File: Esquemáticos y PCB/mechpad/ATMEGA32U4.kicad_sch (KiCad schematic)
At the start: 22 parts

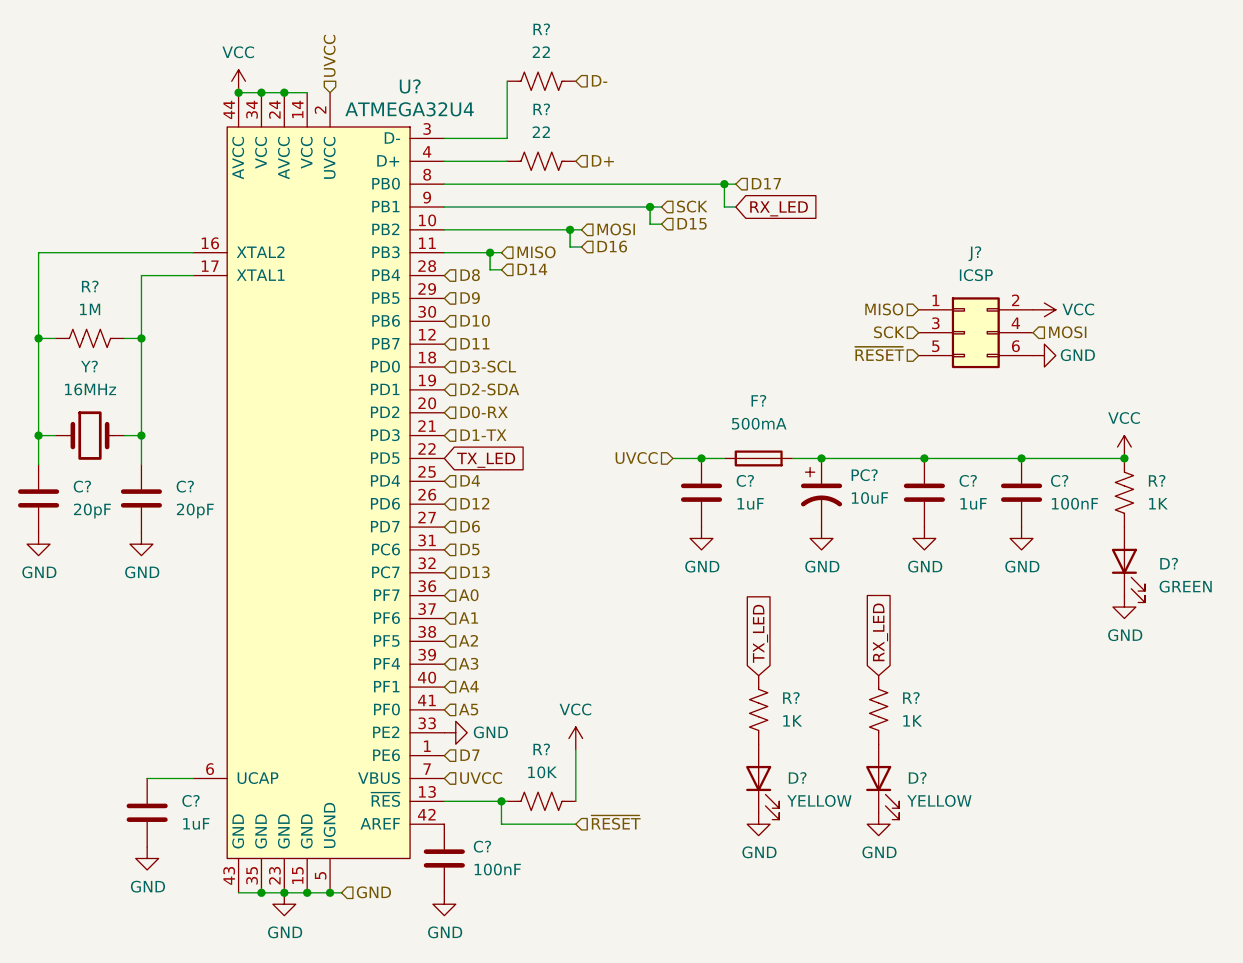
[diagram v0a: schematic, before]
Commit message: Updated schematic
Added connections between hierarchical sheets, more code testing
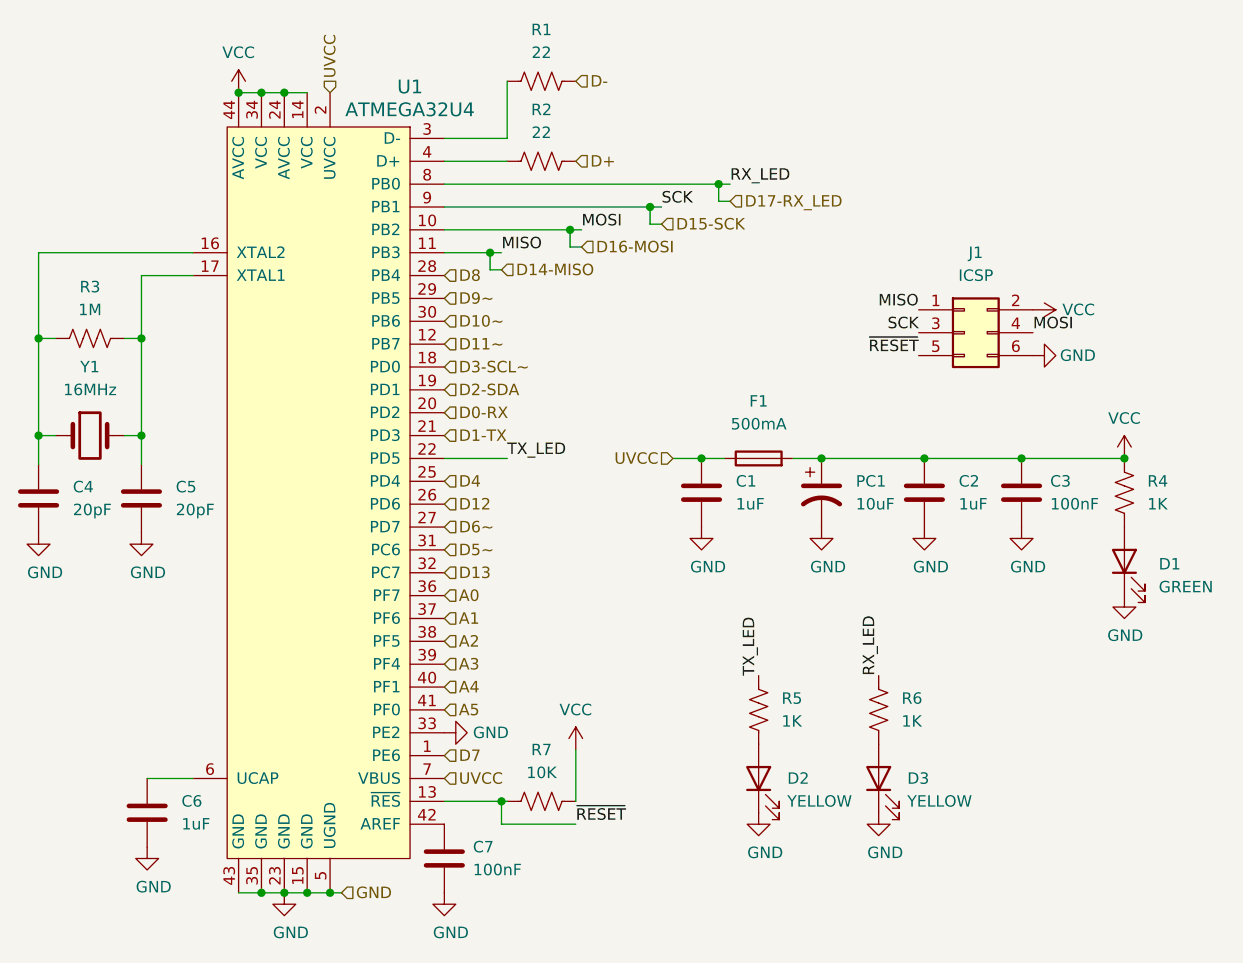
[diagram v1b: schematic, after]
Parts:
- gave numbers to parts that had none: 22
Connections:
- net D10 renamed D10~
- net D11 renamed D11~
- net D14 renamed D14-MISO
- net D15 renamed D15-SCK
- net D16 renamed D16-MOSI
- net D3-SCL renamed D3-SCL~
- net D5 renamed D5~
- net D6 renamed D6~
- net D9 renamed D9~
- net RX_LED renamed D17-RX_LED
